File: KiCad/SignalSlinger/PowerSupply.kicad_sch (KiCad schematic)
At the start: 31 parts, among them J201 Barrel_Jack_Switch, J202 Conn_01x03, U201 LP2985-3.3, U202 LP2985-3.3, U203 TPS63060

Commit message: Updates
o Updated Gerbers
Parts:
- added C216: 10uF, Capacitor_SMD:C_0805_2012Metric, symbol Device:C_Small
- added J203: External Power Source, Connector_PinHeader_2.54mm:PinHeader_1x02_P2.54mm_Vertical, symbol Connector_Generic:Conn_01x02
- added J204: Controlled Power, Connector_PinHeader_2.54mm:PinHeader_1x02_P2.54mm_Vertical, symbol Connector_Generic:Conn_01x02
- added JP201: V-ext disable, Jumper:SolderJumper-2_P1.3mm_Bridged_RoundedPad1.0x1.5mm, symbol Jumper:SolderJumper_2_Bridged
- added U204: TPS22810DBVT, Package_TO_SOT_SMD:SOT-23-6, symbol Power_Management:TPS22810DBVT
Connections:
- net GND: now also C216.2, J203.1 (Pin_1), J204.1 (Pin_1), U204.2 (GND)
- net V_ext: now also JP201.1 (A)
- new net: C216.1, J203.2 (Pin_2), JP201.2 (B), U204.1 (VIN)
- new net: J204.2 (Pin_2), U204.6 (VOUT)
- new net Fan_Contr: U204.3 (EN/UVLO)
- no-connect marks 1 -> 3
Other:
- note added: "OPTIONAL AUX CONTROL"
- moved on the sheet: BT201, C201, C202, C203, C204, C205, C206, C207, C208, C209, C210, C211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

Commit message: KiCad Updates
Updated Gerbers and schematic
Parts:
- C213, C214, C215: footprint Capacitor_SMD:C_1210_3225Metric -> Capacitor_SMD:C_0805_2012Metric
- L201: footprint Inductor_SMD:L_Wuerth_WE-LQS -> Inductor_SMD:WPN4020H2R2MT; Digi-Key Part No. 732-10754-1-ND -> 3442-WPN4020H2R2MTCT-ND; LCSC Part Number C2041406 -> (none); Link https://www.digikey.com/en/products/detail/w%C3%BCrth-elekt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 -> https://www.digikey.com/en/products/detail/shenzhen-sunlord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; Manufacturer Würth Elektronik -> Shenzhen Sunlord Electronics Co., Ltd.; Manufacturer PN 74404043022A -> WPN4020H2R2MT
- R205: LCSC Part Number (none) -> C273877
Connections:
- net +3V3: now also R204.1
- net +5V: no longer R204.1
- net B/B_PS_Enable: now also R205.2; no longer R205.1
- net GND: now also R205.1; no longer R205.2
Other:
- moved on the sheet: R204

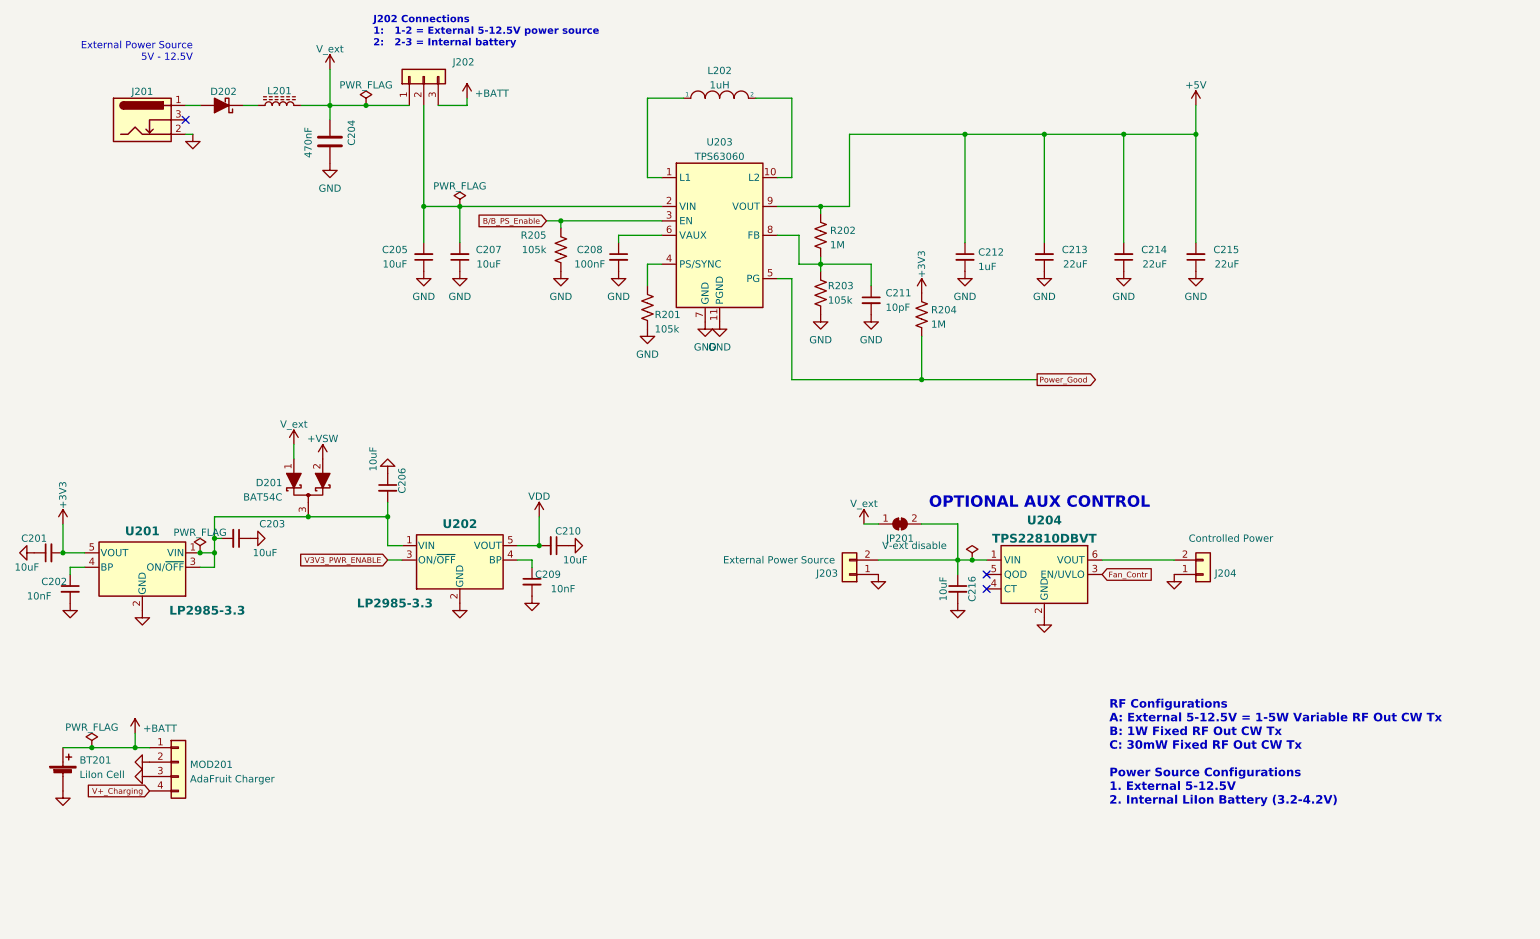
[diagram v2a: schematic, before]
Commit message: Schematic Updates
o Added support for a linear adjustable voltage regulator
o Added a switch
o Re-arranged components for a better fit
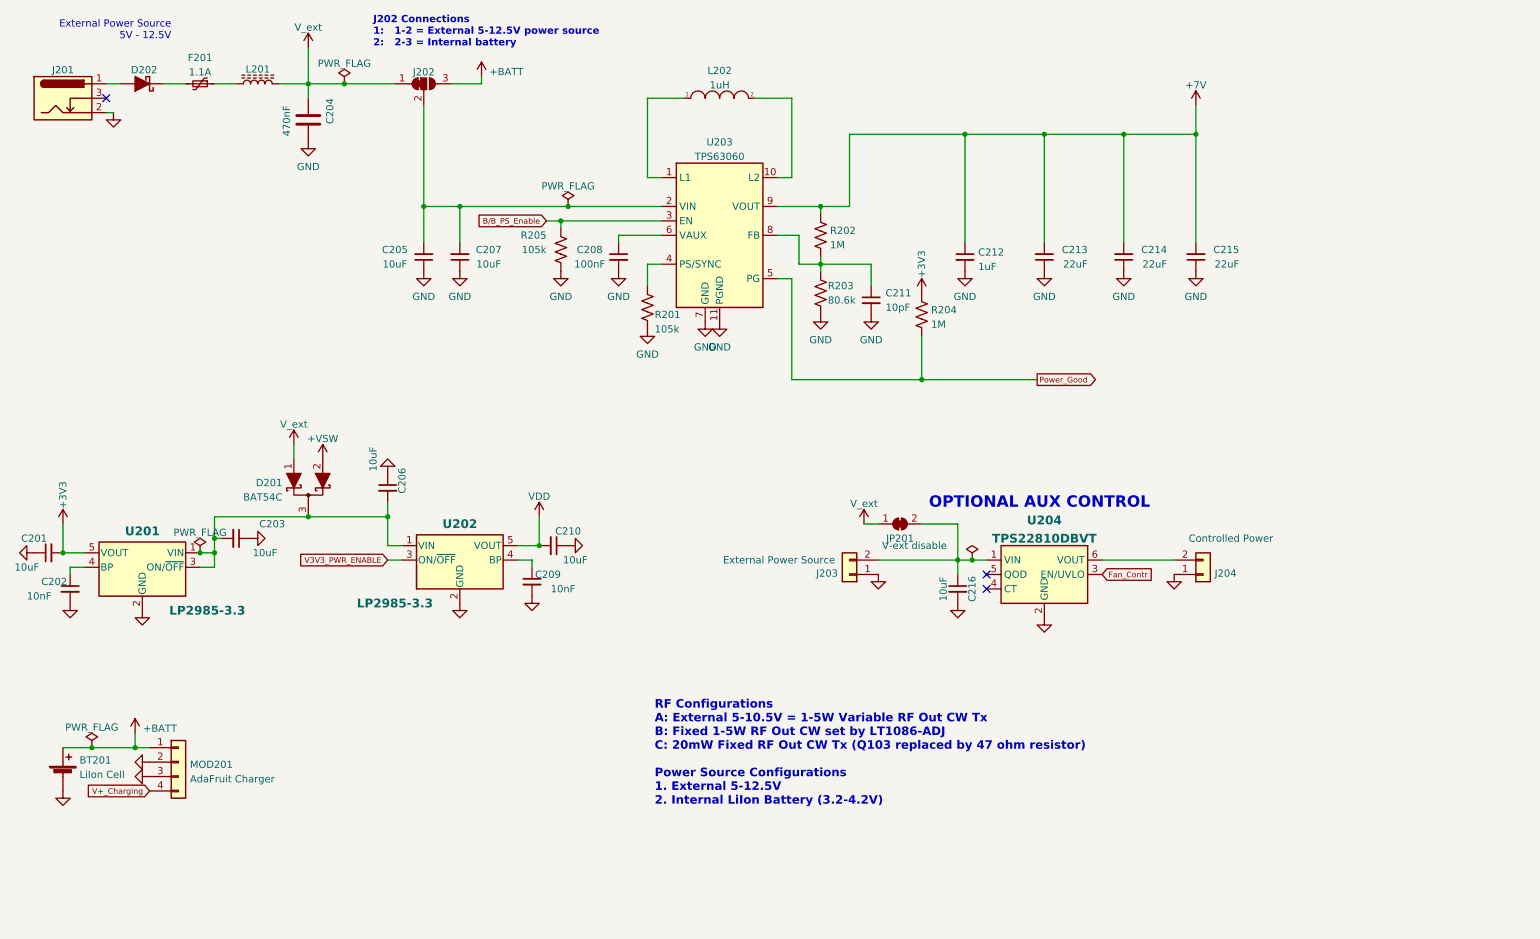
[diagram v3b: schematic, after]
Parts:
- removed J202: Conn_01x03, Connector_PinHeader_2.54mm:PinHeader_1x03_P2.54mm_Vertical, symbol Connector_Generic:Conn_01x03
- added F201: 1.1A, Fuse:Fuse_1812_4532Metric, symbol Device:Polyfuse_Small
- added J202: SolderJumper_3_Bridged12, Jumper:SolderJumper-3_P1.3mm_Bridged12_RoundedPad1.0x1.5mm_NumberLabels, symbol Jumper:SolderJumper_3_Bridged12
- R203: value 105k -> 80.6k; Digi-Key Part No. 311-105KCRCT-ND -> 311-80.6KCRCT-ND; LCSC Part Number C273877 -> (none); Link https://www.digikey.com/en/products/detail/yageo/RC0805FR-07105KL/727548 -> https://www.digikey.com/en/products/detail/yageo/RC0805FR-0780K6L/728161; Manufacturer PN RC0805FR-07105KL -> RC0805FR-0780K6L
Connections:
- net +BATT: now also J202.3 (B)
- net V_ext: now also J202.1 (A)
- net at C205.2, C207.2, U203.2 (VIN): now also J202.2 (C)
- net at L201.1: now also F201.1; no longer D202.1 (K)
- net +5V renamed +7V
- new net: D202.1 (K), F201.2
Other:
- note added: "RF Configurations A: External 5-10.5V = 1-5W Variable RF Out CW Tx B: Fixed 1-5W RF Out CW set by LT1086-ADJ C: 20mW Fixed RF Out CW Tx (Q103 replaced by 47 ohm resistor) Power Source Configurations 1. External 5-12.5V 2. Internal LiIon Battery (3.2-4.2V)"
- note removed: "RF Configurations A: External 5-12.5V = 1-5W Variable RF Out CW Tx B: 1W Fixed RF Out CW Tx C: 30mW Fixed RF Out CW Tx Power Source Configurations 1. External 5-12.5V 2. Internal LiIon Battery (3.2-4.2V)"
- moved on the sheet: C204, D202, J201, L201

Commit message: Updated Schematic Rev
Rev 1.2
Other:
- title: SignalSlinger Design -> SignalSlinger
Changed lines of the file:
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@@
   (paper "A4")
   (title_block
-    (title "SignalSlinger Design")
-    (date "2023-07-10")
-    (rev "1.1")
+    (title "SignalSlinger")
+    (date "2023-11-17")
+    (rev "1.2")
   )
   (junction (at 187.96 116.84) (diameter 0) (color 0 0 0 0)

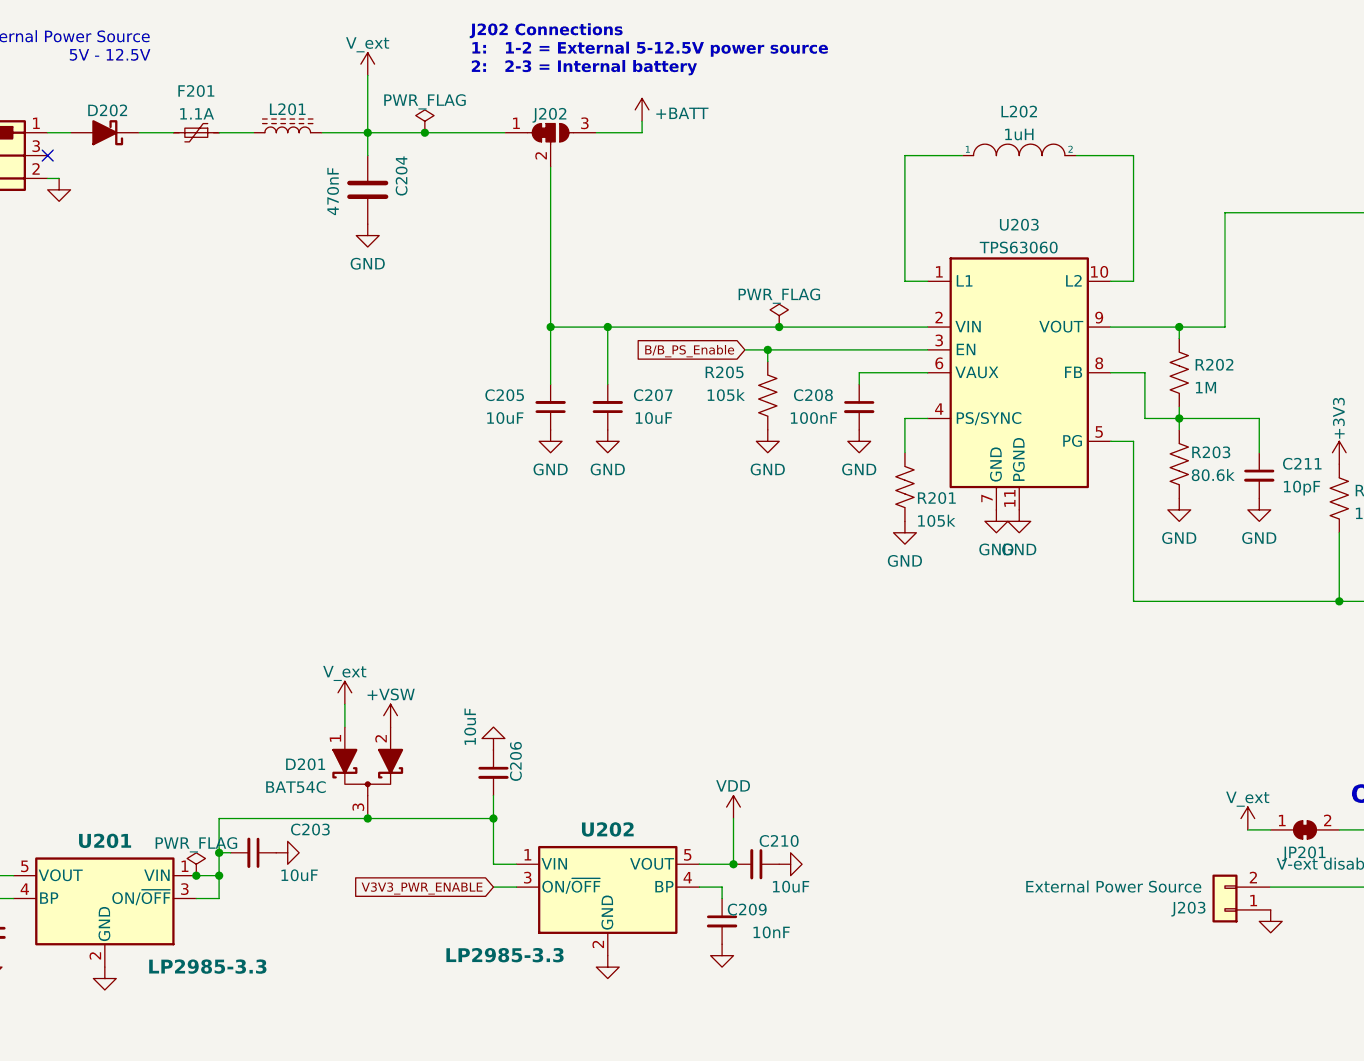
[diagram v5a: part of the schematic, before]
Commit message: KiCad Updates
Updated schematic and PCB.
Added diodes to support USB powering the processor and replacing J202
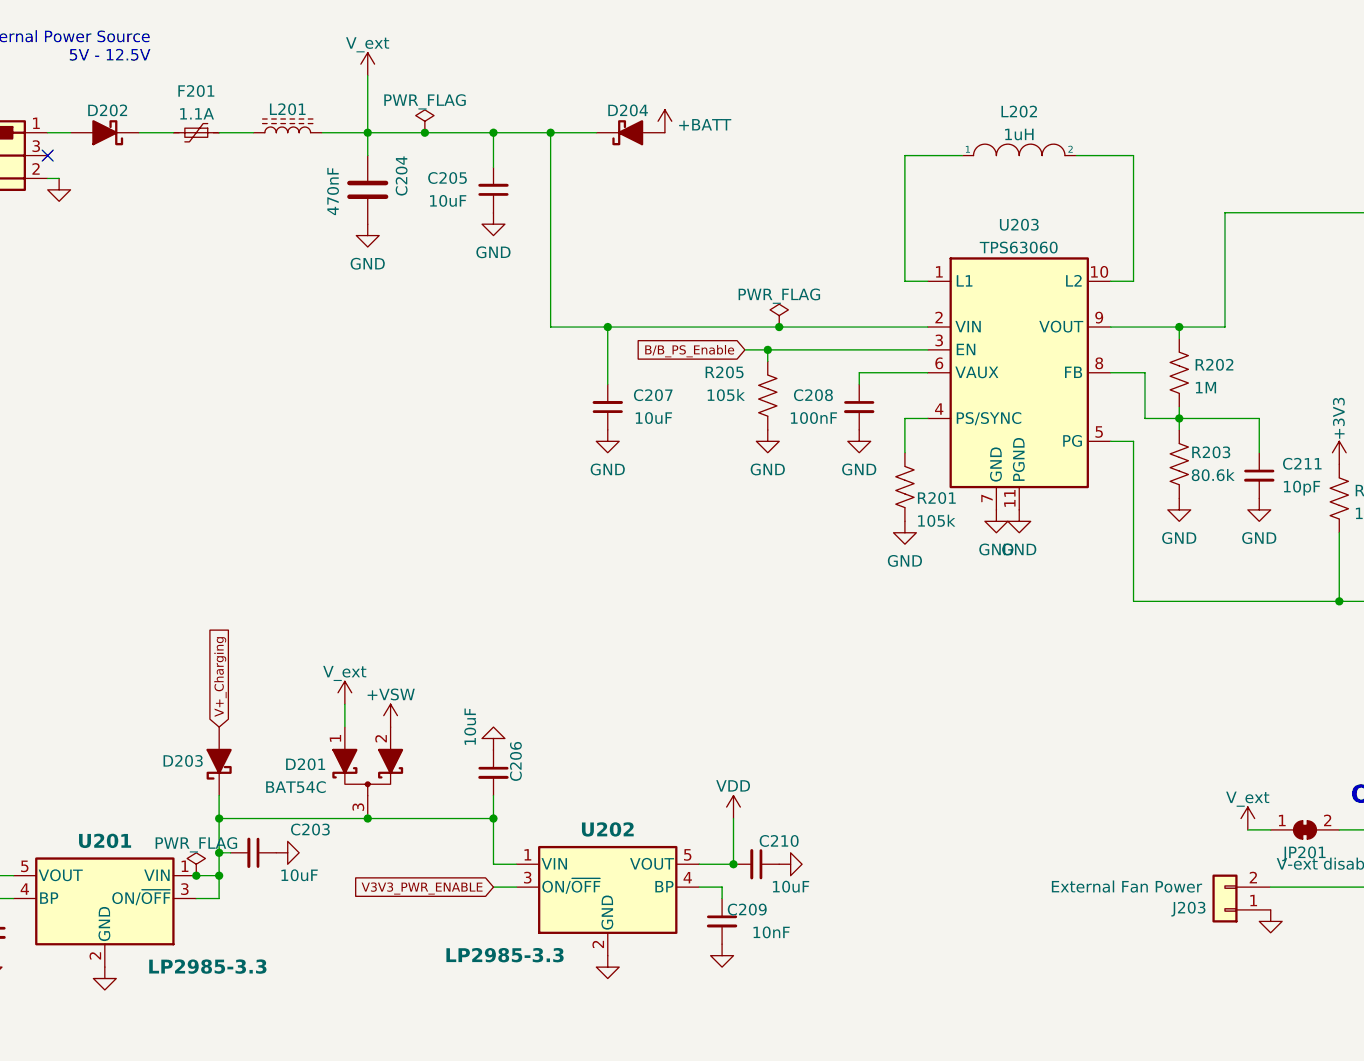
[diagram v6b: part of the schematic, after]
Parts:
- removed J202: SolderJumper_3_Bridged12, Jumper:SolderJumper-3_P1.3mm_Bridged12_RoundedPad1.0x1.5mm_NumberLabels, symbol Jumper:SolderJumper_3_Bridged12
- added D203, D204: (no value), symbol Device:D_Schottky_Filled
- J203: value External Power Source -> External Fan Power
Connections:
- net +BATT: now also D204.2 (A)
- net V+_Charging: now also D203.2 (A)
- net V_ext: now also C205.2, C207.2, U203.2 (VIN), D204.1 (K)
- net at C203.2, C206.2, D201.3 (A)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: now also D203.1 (K)
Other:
- note removed: "J202 Connections 1: 1-2 = External 5-12.5V power source 2: 2-3 = Internal battery"
- moved on the sheet: C205
